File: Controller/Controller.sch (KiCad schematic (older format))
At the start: 22 parts, among them CN1 SERVO_PWM, J1 PJ-202AH, J2 TermLaser, J3 TermStop, J4 LASER_PWR, J5 LASER_PULSE, J6 TermControl, J7 TermLimit, J8 TermAux, J9 ConnPi, U1 CJ7805

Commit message: More power routing
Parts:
- removed J9: ConnPi, Connector_PinHeader_2.54mm:PinHeader_1x05_P2.54mm_Vertical, symbol Connector:Conn_01x05_Female
- removed R7: 1K, OPL_Resistor:R0603, symbol OPL_Resistor:SMD-RES-1K-1%-1_10W_0603_
- removed R8: 2K, OPL_Resistor:R0603, symbol OPL_Resistor:SMD-RES-1K-1%-1_10W_0603_
- added D3: LED_BLUE, OPL_Optoelectronics:LED-0603, symbol OPL_Optoelectronics:SMD-LED-CLEAR-BLUE_0603_
- added R7: 220R, OPL_Resistor:R0603, symbol OPL_Resistor:SMD-RES-220R-5%-1_10W_0603_
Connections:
- net 5V: now also R7.2
- net GND: now also D3.2 (-)
- net GRBL_ABORT: now also J3.3 (Pin_3); no longer J3.1 (Pin_1)
- net NANO_RESET: now also J3.1 (Pin_1); no longer J3.3 (Pin_3)
- new net: D3.1 (+), R7.1
- no-connect marks 8 -> 6
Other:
- note added: "Mounting"
- note removed: "5V"
- note removed: "5V <-> 3.3V\nLevel Shift"
- note removed: "Gnd"
- note removed: "Pi Mounting"
- note removed: "Pi RX"
- note removed: "Pi Serial Interface"
- note removed: "Pi TX"
- moved on the sheet: C1, C2, U1
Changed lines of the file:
@@
 L Regulator_Linear:L7805 U1
 U 1 1 5D4C3827
-P 2550 2850
-F 0 "U1" H 2550 3092 50  0000 C CNN
-F 1 "CJ7805" H 2550 3001 50  0000 C CNN
-F 2 "Package_TO_SOT_SMD:TO-252-2" H 2575 2700 50  0001 L CIN
-F 3 "http://file.elecfans.com/web1/M00/91/C3/pIYBAFzT9eOAVwOtACT5SwN81qY206.pdf?filename=CJ7805%28TO-252-2%29+3%25_JCET.pdf" H 2550 2800 50  0001 C CNN
-F 4 "CJ7805(TO-252-2)" H 2550 2850 50  0001 C CNN "MPN"
-	1    2550 2850
+P 2550 2800
+F 0 "U1" H 2550 3042 50  0000 C CNN
+F 1 "CJ7805" H 2550 2951 50  0000 C CNN
+F 2 "Package_TO_SOT_SMD:TO-252-2" H 2575 2650 50  0001 L CIN
+F 3 "http://file.elecfans.com/web1/M00/91/C3/pIYBAFzT9eOAVwOtACT5SwN81qY206.pdf?filename=CJ7805%28TO-252-2%29+3%25_JCET.pdf" H 2550 2750 50  0001 C CNN
+F 4 "CJ7805(TO-252-2)" H 2550 2800 50  0001 C CNN "MPN"
+	1    2550 2800
 	1    0    0    -1
 $EndComp
@@
 L power:GND #PWR02
 U 1 1 5D4C4526
-P 2550 3150
-F 0 "#PWR02" H 2550 2900 50  0001 C CNN
-F 1 "GND" H 2555 2977 50  0000 C CNN
-F 2 "" H 2550 3150 50  0001 C CNN
-F 3 "" H 2550 3150 50  0001 C CNN
-	1    2550 3150
-	1    0    0    -1
-$EndComp
-Text GLabel 3250 2850 2    31   Input ~ 0
+P 2550 3100
+F 0 "#PWR02" H 2550 2850 50  0001 C CNN
+F 1 "GND" H 2555 2927 50  0000 C CNN
+F 2 "" H 2550 3100 50  0001 C CNN
+F 3 "" H 2550 3100 50  0001 C CNN
+	1    2550 3100
+	1    0    0    -1
+$EndComp
+Text GLabel 3250 2800 2    31   Input ~ 0
 5V
-Text Label 1800 2850 0    31   ~ 0
+Text Label 1800 2800 0    31   ~ 0
 VIN_12V
 $Comp
 L tantalum-smd-10uf-10v-10%_avx-a_:TANTALUM-SMD-10UF-10V-10%_AVX-A_ C?
 U 1 1 5D4CEFF0
-P 2950 3000
+P 2950 2950
 AR Path="/5D499913/5D4CEFF0" Ref="C?"  Part="1"
 AR Path="/5D4AF8B7/5D4CEFF0" Ref="C?"  Part="1"
 AR Path="/5D4CEFF0" Ref="C2"  Part="1"
-F 0 "C2" V 2908 3128 45  0000 L CNN
-F 1 "10uF" V 2992 3128 45  0000 L CNN
-F 2 "Capacitor_Tantalum_SMD:CP_EIA-3216-18_Kemet-A" H 2950 3000 50  0001 C CNN
-F 3 "" H 2950 3000 50  0001 C CNN
-F 4 "TAJA106K010RNJ" H 2980 3150 20  0001 C CNN "MPN"
-F 5 "302020011" H 2980 3150 20  0001 C CNN "SKU"
-	1    2950 3000
+F 0 "C2" V 2908 3078 45  0000 L CNN
+F 1 "10uF" V 2992 3078 45  0000 L CNN
+F 2 "Capacitor_Tantalum_SMD:CP_EIA-3216-18_Kemet-A" H 2950 2950 50  0001 C CNN
+F 3 "" H 2950 2950 50  0001 C CNN
+F 4 "TAJA106K010RNJ" H 2980 3100 20  0001 C CNN "MPN"
+F 5 "302020011" H 2980 3100 20  0001 C CNN "SKU"
+	1    2950 2950
 	0    1    1    0
 $EndComp
 Wire Wire Line
-	1800 2850 2150 2850
-Wire Wire Line
-	2850 2850 2950 2850
-Connection ~ 2950 2850
-Wire Wire Line
-	2950 2850 3250 2850
+	1800 2800 2150 2800
+Wire Wire Line
+	2850 2800 2950 2800
+Connection ~ 2950 2800
+Wire Wire Line
+	2950 2800 3250 2800
 $Comp
 L tantalum-smd-10uf-10v-10%_avx-a_:TANTALUM-SMD-10UF-10V-10%_AVX-A_ C?
 U 1 1 5D4D028E
-P 2150 3000
+P 2150 2950
 AR Path="/5D499913/5D4D028E" Ref="C?"  Part="1"
 AR Path="/5D4AF8B7/5D4D028E" Ref="C?"  Part="1"
 AR Path="/5D4D028E" Ref="C1"  Part="1"
-F 0 "C1" V 2108 3128 45  0000 L CNN
-F 1 "10uF" V 2192 3128 45  0000 L CNN
-F 2 "Capacitor_Tantalum_SMD:CP_EIA-3216-18_Kemet-A" H 2150 3000 50  0001 C CNN
-F 3 "" H 2150 3000 50  0001 C CNN
-F 4 "TAJA106K010RNJ" H 2180 3150 20  0001 C CNN "MPN"
-F 5 "302020011" H 2180 3150 20  0001 C CNN "SKU"
-	1    2150 3000
+F 0 "C1" V 2108 3078 45  0000 L CNN
+F 1 "10uF" V 2192 3078 45  0000 L CNN
+F 2 "Capacitor_Tantalum_SMD:CP_EIA-3216-18_Kemet-A" H 2150 2950 50  0001 C CNN
+F 3 "" H 2150 2950 50  0001 C CNN
+F 4 "TAJA106K010RNJ" H 2180 3100 20  0001 C CNN "MPN"
+F 5 "302020011" H 2180 3100 20  0001 C CNN "SKU"
+	1    2150 2950
 	0    -1   1    0
 $EndComp
-Connection ~ 2150 2850
-Wire Wire Line
-	2150 2850 2250 2850
-Wire Wire Line
-	2150 3150 2550 3150
-Wire Wire Line
-	2550 3150 2950 3150
-Connection ~ 2550 3150
+Connection ~ 2150 2800
+Wire Wire Line
+	2150 2800 2250 2800
+Wire Wire Line
+	2150 3100 2550 3100
+Wire Wire Line
+	2550 3100 2700 3100
+Connection ~ 2550 3100
 Wire Notes Line
 	1750 2500 1750 3450
-Wire Notes Line
-	1750 3450 3400 3450
 Wire Notes Line
 	3400 3450 3400 2500
@@
 Wire Wire Line
 	8350 3650 8700 3650
+Text Label 3950 5000 1    31   ~ 0
+GRBL_ABORT
 Text Label 4150 5000 1    31   ~ 0
-GRBL_ABORT
-Text Label 3950 5000 1    31   ~ 0
 NANO_RESET
 Wire Wire Line
@@
 	4600 5550 5000 5550
 Connection ~ 4600 5550
-$Comp
-L Connector:Conn_01x05_Female J9
-U 1 1 5D5B9335
-P 1900 5200
-F 0 "J9" H 1792 5585 50  0000 C CNN
-F 1 "ConnPi" H 1792 5494 50  0000 C CNN
-F 2 "Connector_PinHeader_2.54mm:PinHeader_1x05_P2.54mm_Vertical" H 1900 5200 50  0001 C CNN
-F 3 "~" H 1900 5200 50  0001 C CNN
-	1    1900 5200
-	-1   0    0    -1
-$EndComp
-$Comp
-L power:GND #PWR033
-U 1 1 5D5BC623
-P 2200 5200
-F 0 "#PWR033" H 2200 4950 50  0001 C CNN
-F 1 "GND" V 2205 5072 50  0000 R CNN
-F 2 "" H 2200 5200 50  0001 C CNN
-F 3 "" H 2200 5200 50  0001 C CNN
-	1    2200 5200
-	0    -1   -1   0
-$EndComp
-Wire Wire Line
-	2100 5200 2200 5200
-Text Label 2600 5300 2    31   ~ 0
-GRBL_RX
-Wire Wire Line
-	2600 5300 2100 5300
-Text Label 3050 4900 2    31   ~ 0
-GRBL_TX
-$Comp
-L OPL_Resistor:SMD-RES-1K-1%-1_10W_0603_ R?
-U 1 1 5D5C4586
-P 2800 5250
-AR Path="/5D499913/5D5C4586" Ref="R?"  Part="1"
-AR Path="/5D4AF8B7/5D5C4586" Ref="R?"  Part="1"
-AR Path="/5D5C4586" Ref="R7"  Part="1"
-F 0 "R7" H 2800 5200 45  0000 C CNN
-F 1 "1K" H 2800 5340 45  0000 C CNN
-F 2 "OPL_Resistor:R0603" H 2800 5250 40  0001 C CNN
-F 3 "" H 2800 5250 40  0001 C CNN
-F 4 "RC0603FR-071KL" H 2830 5400 20  0001 C CNN "MPN"
-F 5 "301010298" H 2830 5400 20  0001 C CNN "SKU"
-	1    2800 5250
-	0    1    1    0
-$EndComp
-$Comp
-L OPL_Resistor:SMD-RES-1K-1%-1_10W_0603_ R?
-U 1 1 5D5C71B6
-P 2800 5550
-AR Path="/5D499913/5D5C71B6" Ref="R?"  Part="1"
-AR Path="/5D4AF8B7/5D5C71B6" Ref="R?"  Part="1"
-AR Path="/5D5C71B6" Ref="R8"  Part="1"
-F 0 "R8" H 2800 5500 45  0000 C CNN
-F 1 "2K" H 2800 5640 45  0000 C CNN
-F 2 "OPL_Resistor:R0603" H 2800 5550 40  0001 C CNN
-F 3 "" H 2800 5550 40  0001 C CNN
-F 4 "RC0603FR-072KL" H 2830 5700 20  0001 C CNN "MPN"
-F 5 "301010221" H 2830 5700 20  0001 C CNN "SKU"
-	1    2800 5550
-	0    1    1    0
-$EndComp
-Wire Wire Line
-	2100 5400 2800 5400
-Connection ~ 2800 5400
-Wire Wire Line
-	2800 5100 2800 4900
-Wire Wire Line
-	2800 4900 3050 4900
-$Comp
-L power:GND #PWR034
-U 1 1 5D5CCAC8
-P 2800 5700
-F 0 "#PWR034" H 2800 5450 50  0001 C CNN
-F 1 "GND" V 2805 5572 50  0000 R CNN
-F 2 "" H 2800 5700 50  0001 C CNN
-F 3 "" H 2800 5700 50  0001 C CNN
-	1    2800 5700
-	1    0    0    -1
-$EndComp
-Text Notes 1800 5000 0    31   ~ 0
-5V
-Text Notes 1800 5100 0    31   ~ 0
-5V
-Text Notes 1750 5200 0    31   ~ 0
-Gnd
-Text Notes 1750 5300 0    31   ~ 0
-Pi TX
-Text Notes 1750 5400 0    31   ~ 0
-Pi RX
-Text Notes 2950 5450 0    31   ~ 0
-5V <-> 3.3V\nLevel Shift
-NoConn ~ 2100 5000
-NoConn ~ 2100 5100
-Wire Notes Line
-	1700 4750 3300 4750
-Wire Notes Line
-	3300 4750 3300 6050
-Wire Notes Line
-	3300 6050 1700 6050
-Wire Notes Line
-	1700 6050 1700 4750
-Text Notes 2100 4700 0    59   ~ 0
-Pi Serial Interface
 Wire Notes Line
 	3450 5650 5350 5650
@@
 	3450 5300 3450 5650
 Text Notes 4150 5250 0    59   ~ 0
-Pi Mounting
+Mounting
 $Comp
 L Mechanical:Fiducial FID1
@@
 	1    0    0    -1
 $EndComp
+Wire Wire Line
+	3000 3900 3000 4000
+$Comp
+L OPL_Optoelectronics:SMD-LED-CLEAR-BLUE_0603_ D?
+U 1 1 5D671A5F
+P 2850 3250
+AR Path="/5D499913/5D671A5F" Ref="D?"  Part="1"
+AR Path="/5D4AF8B7/5D671A5F" Ref="D?"  Part="1"
+AR Path="/5D671A5F" Ref="D3"  Part="1"
+F 0 "D3" H 2700 3200 45  0000 L CNN
+F 1 "LED_BLUE" H 2450 3350 45  0000 L CNN
+F 2 "OPL_Optoelectronics:LED-0603" H 2850 3250 50  0001 C CNN
+F 3 "" H 2850 3250 50  0001 C CNN
+F 4 "19-217-BHC-ZL1M2RY-3T" H 2880 3400 20  0001 C CNN "MPN"
+F 5 "304090045" H 2880 3400 20  0001 C CNN "SKU"
+	1    2850 3250
+	-1   0    0    1
+$EndComp
+$Comp
+L OPL_Resistor:SMD-RES-220R-5%-1_10W_0603_ R?
+U 1 1 5D671A67
+P 3150 3250
+AR Path="/5D499913/5D671A67" Ref="R?"  Part="1"
+AR Path="/5D4AF8B7/5D671A67" Ref="R?"  Part="1"
+AR Path="/5D671A67" Ref="R7"  Part="1"
+F 0 "R7" H 3150 3424 45  0000 C CNN
+F 1 "220R" H 3150 3340 45  0000 C CNN
+F 2 "OPL_Resistor:R0603" H 3150 3336 40  0001 C CNN
+F 3 "" H 3150 3250 40  0001 C CNN
+F 4 "RC0603JR-07220RL" H 3180 3400 20  0001 C CNN "MPN"
+F 5 "301010163" H 3180 3400 20  0001 C CNN "SKU"
+	1    3150 3250
+	1    0    0    -1
+$EndComp
+Wire Notes Line
+	1750 3450 3400 3450
+Wire Wire Line
+	3250 2800 3250 2950
+Wire Wire Line
+	3250 2950 3300 2950
+Wire Wire Line
+	3300 2950 3300 3250
+Wire Wire Line
+	2700 3250 2700 3100
+Connection ~ 2700 3100
+Wire Wire Line
+	2700 3100 2950 3100
 $EndSCHEMATC

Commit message: Mostly final layout
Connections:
- net HOLD: now also J6.1 (Pin_1); no longer J6.3 (Pin_3)
- net START: now also J6.3 (Pin_3); no longer J6.1 (Pin_1)
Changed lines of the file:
@@
 Text Label 5250 4850 1    31   ~ 0
 Y_LIMIT
+Text Label 4600 4850 1    31   ~ 0
+START
 Text Label 4800 4850 1    31   ~ 0
-START
-Text Label 4600 4850 1    31   ~ 0
 HOLD
 $Comp

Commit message: Beta v1
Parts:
- added J15: 12V_TERM, OPL_Connector:H2-5.0-10.5X8.0MM, symbol OPL_Connector:SCREW-TERMINAL-GREEN_2P-5.0_
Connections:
- net GND: now also J15.2
- net VIN_12V: now also J15.1
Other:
- note added: "Power In 12V"
- note removed: "Power In 12-24V\n(Normally 12V for Laser)"
- moved on the sheet: J1
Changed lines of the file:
@@
 L dk_Barrel-Power-Connectors:PJ-202A J1
 U 1 1 5D545F21
-P 2250 4200
-F 0 "J1" H 2183 4425 50  0000 C CNN
-F 1 "PJ-202AH" H 2183 4334 50  0000 C CNN
-F 2 "digikey-footprints:Barrel_Jack_5.5mmODx2.1mmID_PJ-202A" H 2450 4400 60  0001 L CNN
-F 3 "https://www.cui.com/product/resource/digikeypdf/pj-202ah.pdf" H 2450 4500 60  0001 L CNN
-F 4 "CP-202AH-ND" H 2450 4600 60  0001 L CNN "Digi-Key_PN"
-F 5 "PJ-202AH" H 2450 4700 60  0001 L CNN "MPN"
-F 6 "Connectors, Interconnects" H 2450 4800 60  0001 L CNN "Category"
-F 7 "Barrel - Power Connectors" H 2450 4900 60  0001 L CNN "Family"
-F 8 "https://www.cui.com/product/resource/digikeypdf/pj-202ah.pdf" H 2450 5000 60  0001 L CNN "DK_Datasheet_Link"
-F 9 "https://www.digikey.com/product-detail/en/cui-inc/PJ-202AH/CP-202AH-ND/408450" H 2450 5100 60  0001 L CNN "DK_Detail_Page"
-F 10 "CONN PWR JACK 2X5.5MM KINKED PIN" H 2450 5200 60  0001 L CNN "Description"
-F 11 "CUI Inc." H 2450 5300 60  0001 L CNN "Manufacturer"
-F 12 "Active" H 2450 5400 60  0001 L CNN "Status"
-	1    2250 4200
+P 2700 4000
+F 0 "J1" H 2633 4225 50  0000 C CNN
+F 1 "PJ-202AH" H 2633 4134 50  0000 C CNN
+F 2 "digikey-footprints:Barrel_Jack_5.5mmODx2.1mmID_PJ-202A" H 2900 4200 60  0001 L CNN
+F 3 "https://www.cui.com/product/resource/digikeypdf/pj-202ah.pdf" H 2900 4300 60  0001 L CNN
+F 4 "CP-202AH-ND" H 2900 4400 60  0001 L CNN "Digi-Key_PN"
+F 5 "PJ-202AH" H 2900 4500 60  0001 L CNN "MPN"
+F 6 "Connectors, Interconnects" H 2900 4600 60  0001 L CNN "Category"
+F 7 "Barrel - Power Connectors" H 2900 4700 60  0001 L CNN "Family"
+F 8 "https://www.cui.com/product/resource/digikeypdf/pj-202ah.pdf" H 2900 4800 60  0001 L CNN "DK_Datasheet_Link"
+F 9 "https://www.digikey.com/product-detail/en/cui-inc/PJ-202AH/CP-202AH-ND/408450" H 2900 4900 60  0001 L CNN "DK_Detail_Page"
+F 10 "CONN PWR JACK 2X5.5MM KINKED PIN" H 2900 5000 60  0001 L CNN "Description"
+F 11 "CUI Inc." H 2900 5100 60  0001 L CNN "Manufacturer"
+F 12 "Active" H 2900 5200 60  0001 L CNN "Status"
+	1    2700 4000
 	1    0    0    -1
 $EndComp
@@
 L power:GND #PWR01
 U 1 1 5D546925
-P 2350 4400
-F 0 "#PWR01" H 2350 4150 50  0001 C CNN
-F 1 "GND" V 2355 4272 50  0000 R CNN
-F 2 "" H 2350 4400 50  0001 C CNN
-F 3 "" H 2350 4400 50  0001 C CNN
-	1    2350 4400
+P 2800 4200
+F 0 "#PWR01" H 2800 3950 50  0001 C CNN
+F 1 "GND" V 2805 4072 50  0000 R CNN
+F 2 "" H 2800 4200 50  0001 C CNN
+F 3 "" H 2800 4200 50  0001 C CNN
+	1    2800 4200
 	0    -1   -1   0
 $EndComp
 Wire Wire Line
-	2350 4300 2350 4400
-Connection ~ 2350 4400
-Text Label 2600 4200 2    31   ~ 0
+	2800 4100 2800 4200
+Connection ~ 2800 4200
+Text Label 3050 4000 2    31   ~ 0
 VIN_12V
 Wire Wire Line
-	2350 4200 2600 4200
-Wire Notes Line
-	1850 3900 2750 3900
-Wire Notes Line
-	2750 3900 2750 4500
-Wire Notes Line
-	2750 4500 1850 4500
-Wire Notes Line
-	1850 4500 1850 3900
-Text Notes 1750 3800 0    59   ~ 0
-Power In 12-24V\n(Normally 12V for Laser)
+	2800 4000 3050 4000
+Text Notes 2100 3650 0    59   ~ 0
+Power In 12V
 $Comp
 L power:PWR_FLAG #FLG0101
@@
 	1    0    0    -1
 $EndComp
-Wire Wire Line
-	3000 3900 3000 4000
 $Comp
 L OPL_Optoelectronics:SMD-LED-CLEAR-BLUE_0603_ D?
@@
 Wire Wire Line
 	2700 3100 2950 3100
+$Comp
+L OPL_Connector:SCREW-TERMINAL-GREEN_2P-5.0_ J15
+U 1 1 5D526D9B
+P 1900 4100
+F 0 "J15" H 1842 4454 45  0000 C CNN
+F 1 "12V_TERM" H 1842 4370 45  0000 C CNN
+F 2 "OPL_Connector:H2-5.0-10.5X8.0MM" H 1900 4100 50  0001 C CNN
+F 3 "" H 1900 4100 50  0001 C CNN
+F 4 "320110031" H 1930 4250 20  0001 C CNN "SKU"
+	1    1900 4100
+	-1   0    0    -1
+$EndComp
+$Comp
+L power:GND #PWR0101
+U 1 1 5D52A8E4
+P 2100 4200
+F 0 "#PWR0101" H 2100 3950 50  0001 C CNN
+F 1 "GND" V 2105 4072 50  0000 R CNN
+F 2 "" H 2100 4200 50  0001 C CNN
+F 3 "" H 2100 4200 50  0001 C CNN
+	1    2100 4200
+	0    -1   -1   0
+$EndComp
+Text Label 2350 4000 2    31   ~ 0
+VIN_12V
+Wire Wire Line
+	2100 4000 2350 4000
+Wire Notes Line
+	1750 3700 3100 3700
+Wire Notes Line
+	3100 4350 1750 4350
+Wire Notes Line
+	1750 4350 1750 3700
+Wire Notes Line
+	3100 3700 3100 4350
 $EndSCHEMATC

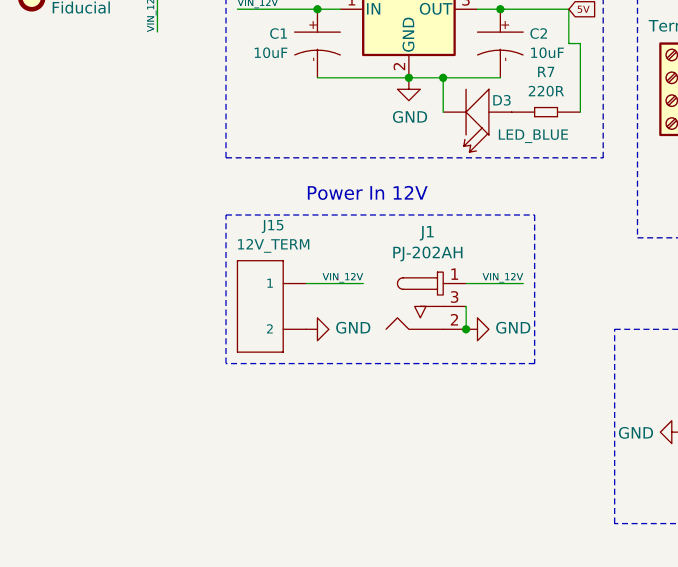
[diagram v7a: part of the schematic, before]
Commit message: Finished adding 3D models
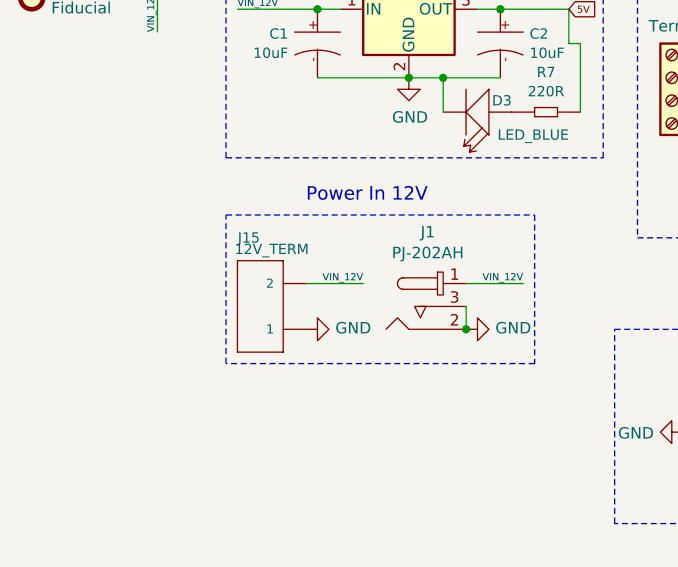
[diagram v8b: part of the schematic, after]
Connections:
- net GND: now also J15.1; no longer J15.2
- net VIN_12V: now also J15.2; no longer J15.1
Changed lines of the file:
@@
 U 1 1 5D526D9B
 P 1900 4100
-F 0 "J15" H 1842 4454 45  0000 C CNN
-F 1 "12V_TERM" H 1842 4370 45  0000 C CNN
+F 0 "J15" H 1950 3800 45  0000 C CNN
+F 1 "12V_TERM" H 1850 3850 45  0000 C CNN
 F 2 "OPL_Connector:H2-5.0-10.5X8.0MM" H 1900 4100 50  0001 C CNN
 F 3 "" H 1900 4100 50  0001 C CNN
 F 4 "320110031" H 1930 4250 20  0001 C CNN "SKU"
 	1    1900 4100
-	-1   0    0    -1
+	-1   0    0    1
 $EndComp
 $Comp
